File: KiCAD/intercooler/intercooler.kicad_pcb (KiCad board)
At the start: 2 copper layers, 53 x 30 mm, 4 parts, among them J1 Conn_01x01_Socket, J2 Conn_01x01_Socket

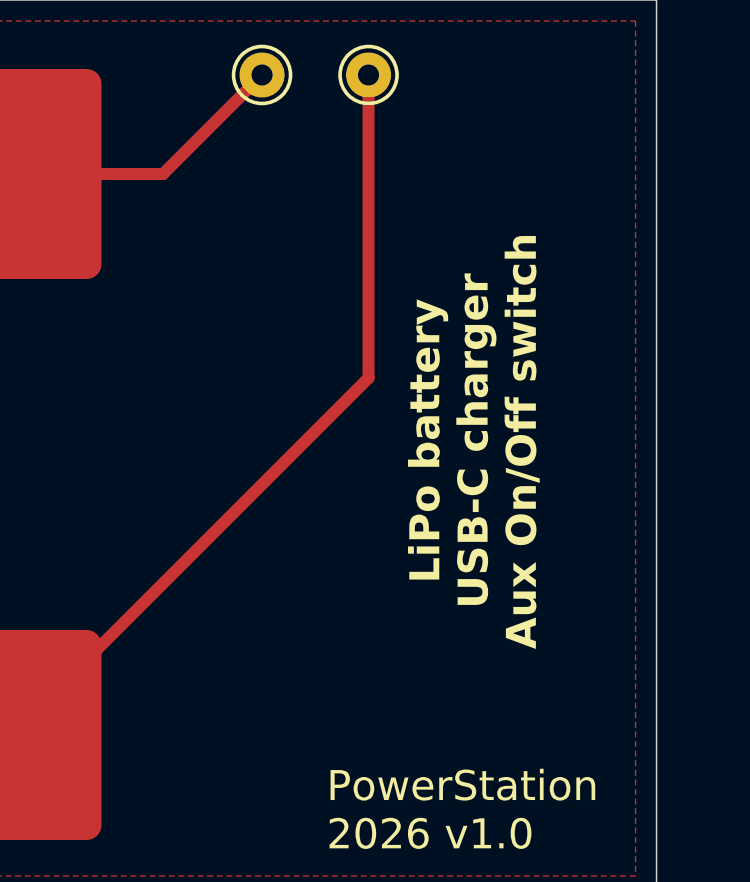
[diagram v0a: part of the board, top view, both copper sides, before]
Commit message: v1.0: Bestilt hos JLCPCB 260626
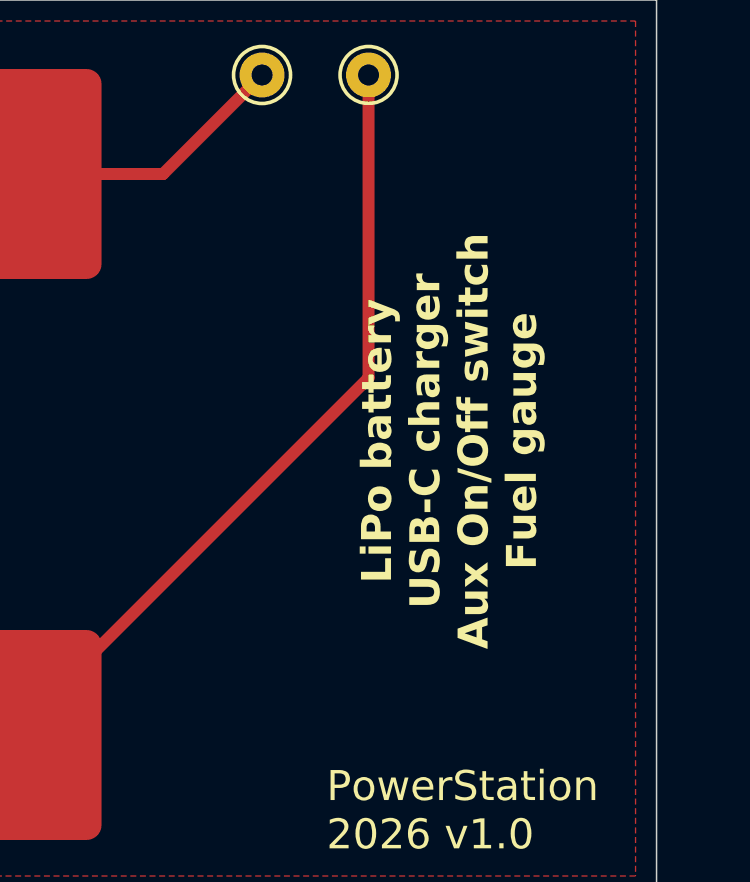
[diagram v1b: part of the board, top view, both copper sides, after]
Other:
- board text added: "LiPo battery USB-C charger Aux On/Off switch Fuel gauge"
- board text removed: "LiPo battery USB-C charger Aux On/Off switch"
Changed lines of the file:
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@@
 		)
 	)
-	(gr_text "LiPo battery\nUSB-C charger\nAux On/Off switch"
+	(gr_text "LiPo battery\nUSB-C charger\nAux On/Off switch\nFuel gauge"
 		(at 149.1 114.7 90)
 		(layer "F.SilkS")
